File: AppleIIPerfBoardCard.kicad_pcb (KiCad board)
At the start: 2 copper layers, 177.8 x 77.5 mm, 1663 parts, among them J1 Conn_02x25_Counter_Clockwise, J2 50_POS_Card_Edge_Connector

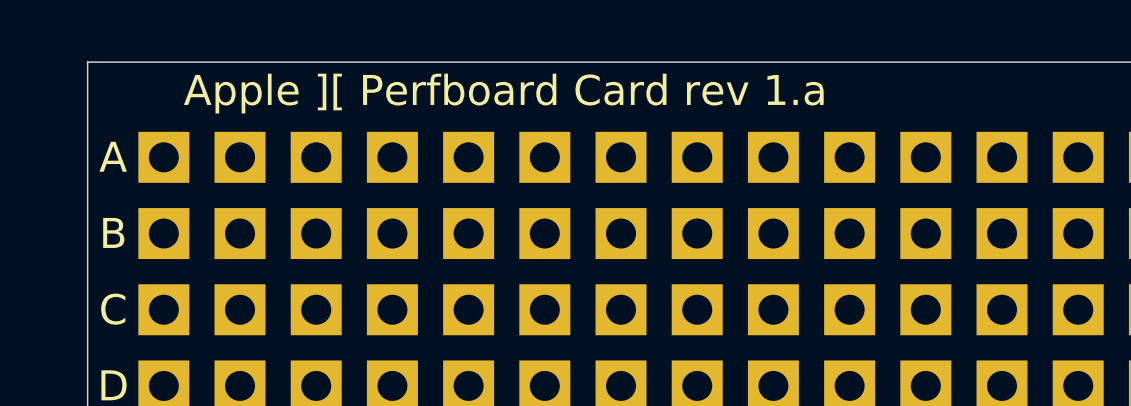
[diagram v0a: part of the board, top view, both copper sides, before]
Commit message: updated silkscreen to rev 1.b
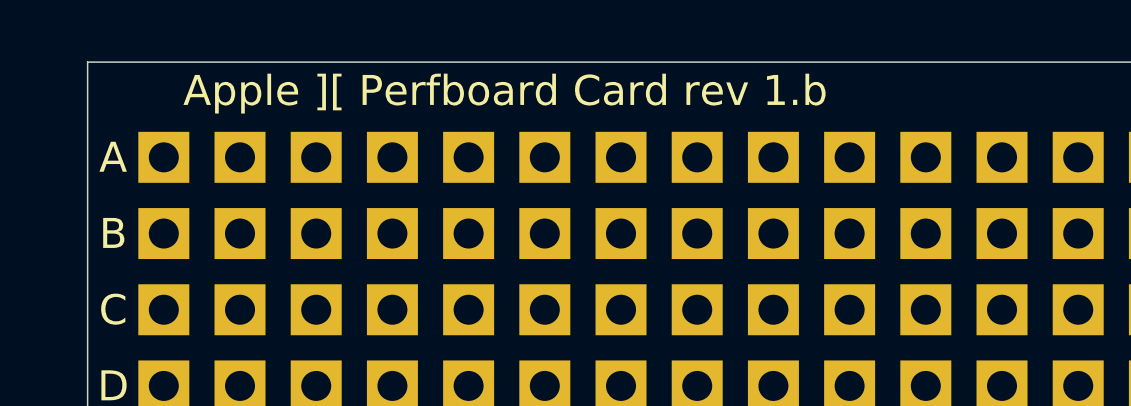
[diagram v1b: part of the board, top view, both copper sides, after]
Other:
- board text added: "Apple ][ Perfboard Card rev 1.b"
- board text removed: "Apple ][ Perfboard Card rev 1.a"
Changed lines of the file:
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@@
     (effects (font (size 1 1) (thickness 0.15)))
   )
-  (gr_text "Apple ][ Perfboard Card rev 1.a" (at 68.92036 61.26226) (layer F.SilkS)
+  (gr_text "Apple ][ Perfboard Card rev 1.b" (at 68.92036 61.26226) (layer F.SilkS)
     (effects (font (size 1 1) (thickness 0.15)))
   )
